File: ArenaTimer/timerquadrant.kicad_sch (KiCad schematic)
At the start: 35 parts

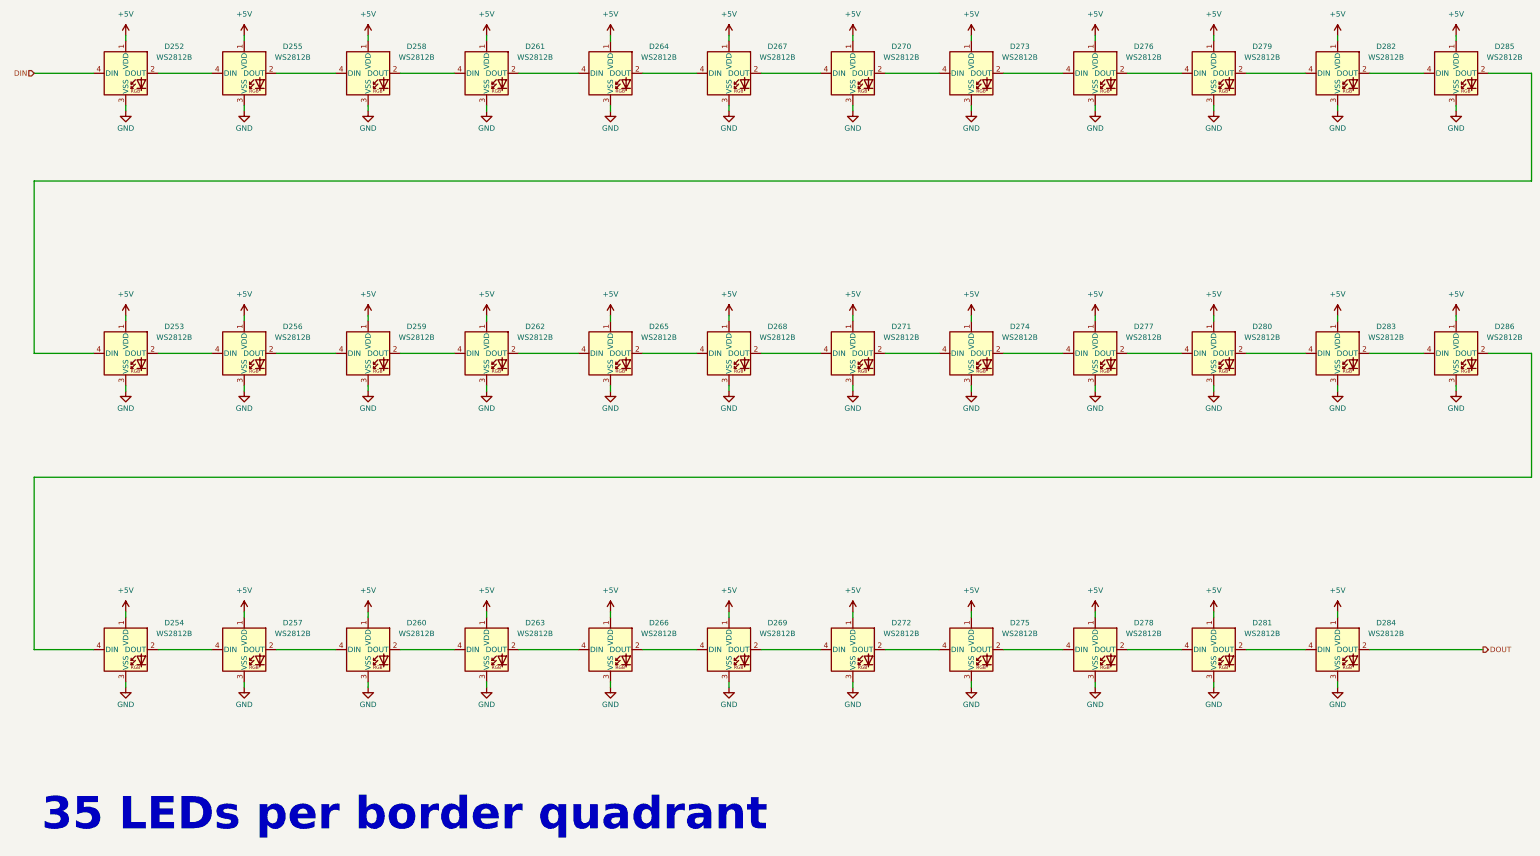
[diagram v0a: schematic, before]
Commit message: PCB changes, code for TRC timers
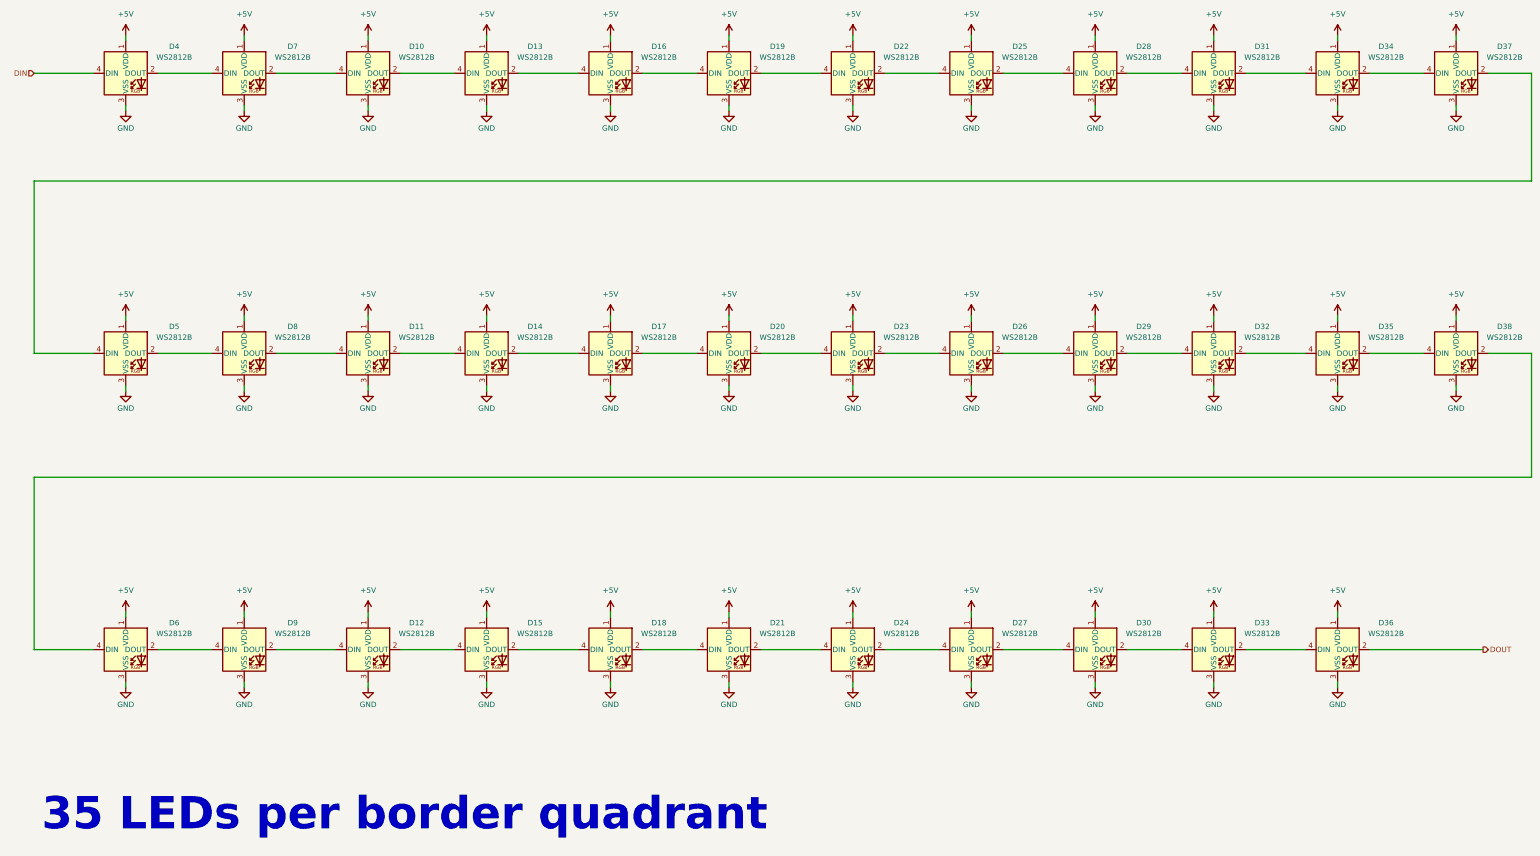
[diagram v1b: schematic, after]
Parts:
- renumbered D258 to D10, D259 to D11, D260 to D12, D261 to D13, D262 to D14, D263 to D15, D264 to D16, D265 to D17, D266 to D18, D267 to D19, D268 to D20, D269 to D21, D270 to D22, D271 to D23, D272 to D24, D273 to D25, D274 to D26, D275 to D27, D276 to D28, D277 to D29, D278 to D30, D279 to D31, D280 to D32, D281 to D33, D282 to D34, D283 to D35, D284 to D36, D285 to D37, D286 to D38, D252 to D4, D253 to D5, D254 to D6, D255 to D7, D256 to D8, D257 to D9
